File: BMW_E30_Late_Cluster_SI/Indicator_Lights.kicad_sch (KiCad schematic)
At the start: 20 parts, among them J1 SI LED Board, Q19 BC337-25, Q21 BC337-25, Q22 BC337-25, Q23 BC337-25, Y2 Crystal

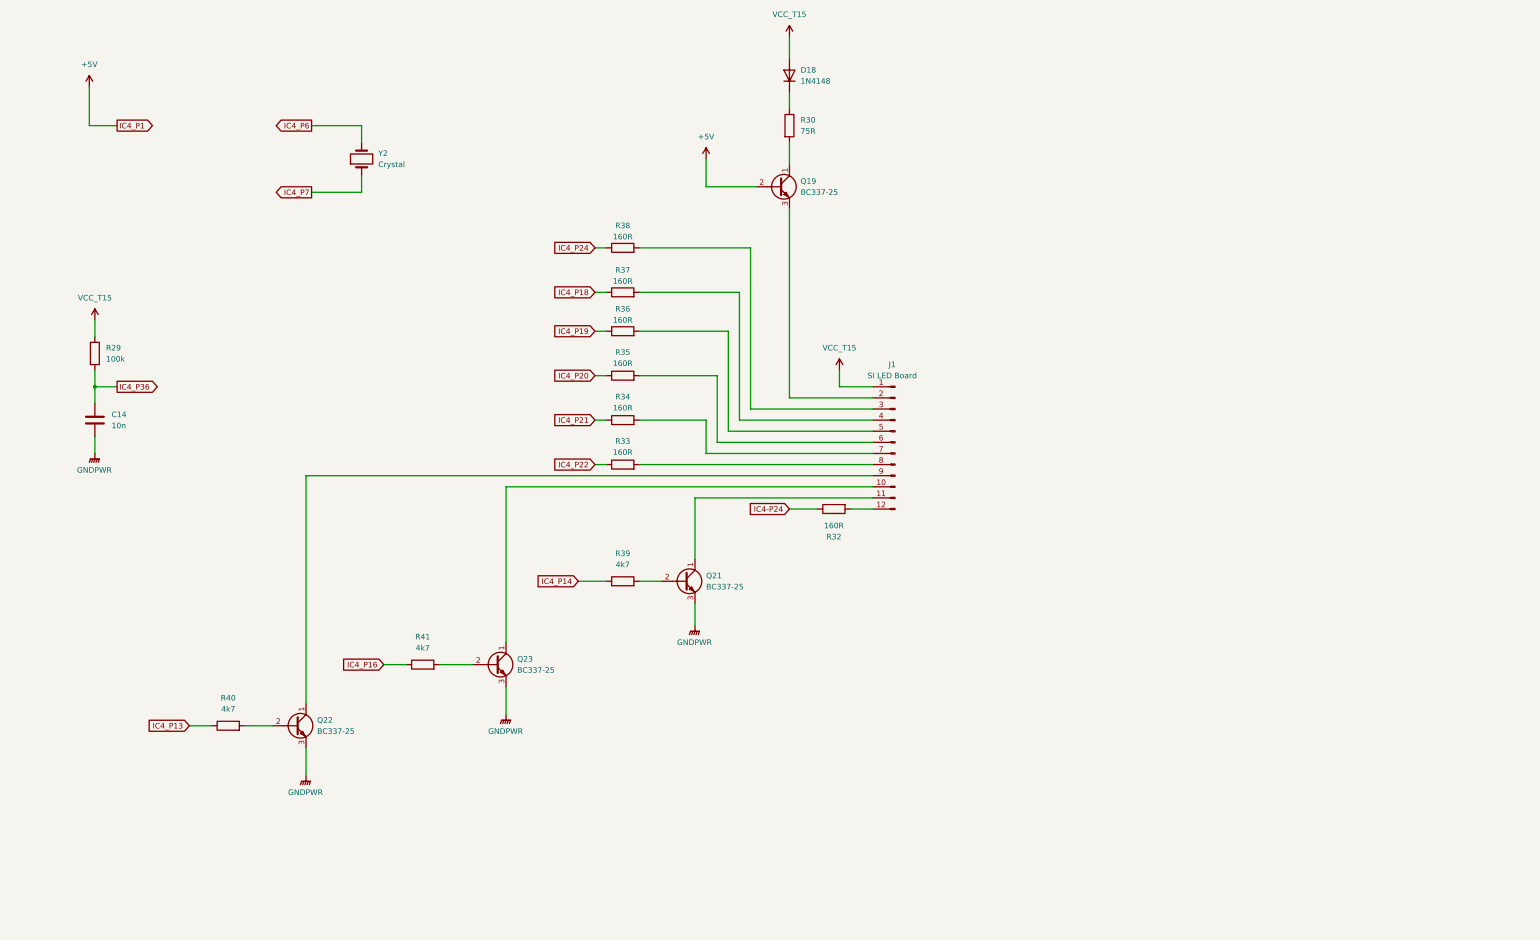
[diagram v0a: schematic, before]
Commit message: IC's Added to Schematic
IC's added, started going through IC2 (U2), pinouts not complete for these yet as many pins go between chips with no other components involved.
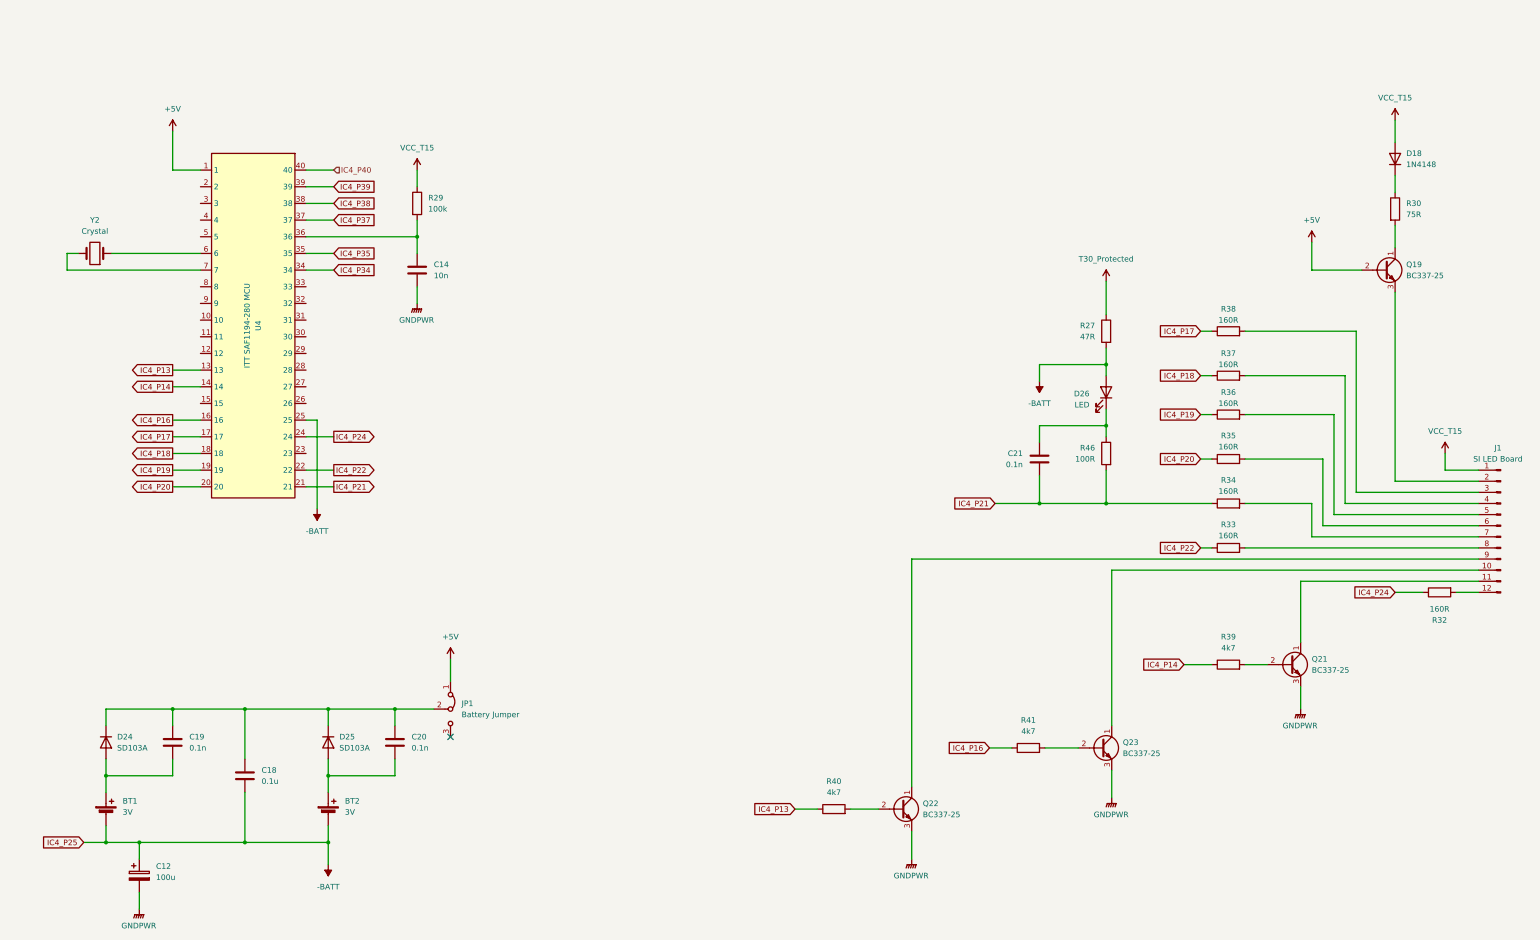
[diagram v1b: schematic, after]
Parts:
- added BT1, BT2: 3V, symbol Device:Battery_Cell
- added C12: 100u, Capacitor_THT:CP_Axial_L18.0mm_D6.5mm_P25.00mm_Horizontal, symbol Device:C_Polarized
- added C18: 0.1u, Capacitor_THT:C_Rect_L7.0mm_W2.0mm_P5.00mm, symbol Device:C
- added C19, C20, C21: 0.1n, Capacitor_THT:C_Disc_D6.0mm_W2.5mm_P5.00mm, symbol Device:C
- added D24, D25: SD103A, symbol Device:D
- added D26: LED, symbol Device:LED
- added JP1: Battery Jumper, symbol Jumper:Jumper_3_Bridged12
- added R27: 47R, Resistor_THT:R_Axial_DIN0516_L15.5mm_D5.0mm_P20.32mm_Horizontal, symbol Device:R
- added R46: 100R, SI_THT:R_Axial_Narrow_L6.8mm_D2.4mm_P9.7mm, symbol Device:R
- added U4: ITT SAF1194-280 MCU, Package_DIP:DIP-40_W15.24mm_LongPads, symbol BMW_ICs:ITT_SAF1194-280_MCU
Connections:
- net IC4-P24 is gone; now on net IC4_P24: R32.1
- net +5V: now also JP1.1 (A), U4.1
- net GNDPWR: now also C12.2
- net IC4_P13: now also U4.13
- net IC4_P14: now also U4.14
- net IC4_P16: now also U4.16
- net IC4_P18: now also U4.18
- net IC4_P19: now also U4.19
- net IC4_P20: now also U4.20
- net IC4_P21: now also C21.2, R46.2, U4.21
- net IC4_P22: now also U4.22
- net IC4_P24: now also U4.24; no longer R38.1
- net IC4_P36: no longer names the net of C14.1, R29.2
- net IC4_P36: now also U4.36
- net IC4_P6: no longer names the net of Y2.2
- net IC4_P6: now also U4.7
- net IC4_P7: no longer names the net of Y2.1
- net IC4_P7: now also U4.6
- new net: C21.1, D26.1 (K), R46.1
- new net: C18.1, C19.1, C20.1, D24.1 (K), D25.1 (K), JP1.2 (C)
- new net: BT2.1 (+), C20.2, D25.2 (A)
- new net: BT1.1 (+), C19.2, D24.2 (A)
- new net -BATT: BT1.2 (-), BT2.2 (-), C12.1, C18.2, D26.2 (A), R27.2, U4.25
- new net IC4_P17: R38.1, U4.17
- new net IC4_P34: U4.34
- new net IC4_P35: U4.35
- new net IC4_P37: U4.37
- new net IC4_P38: U4.38
- new net IC4_P39: U4.39
- new net IC4_P40: U4.40
- new net T30_Protected: R27.1
- no-connect marks 0 -> 1
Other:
- moved on the sheet: C14, D18, J1, Q19, Q21, Q22, Q23, R29, R30, R32, R33, R34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

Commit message: Schematic Functionally Complete
Only changes that should need to be made are formatting and style changes to improve readability.
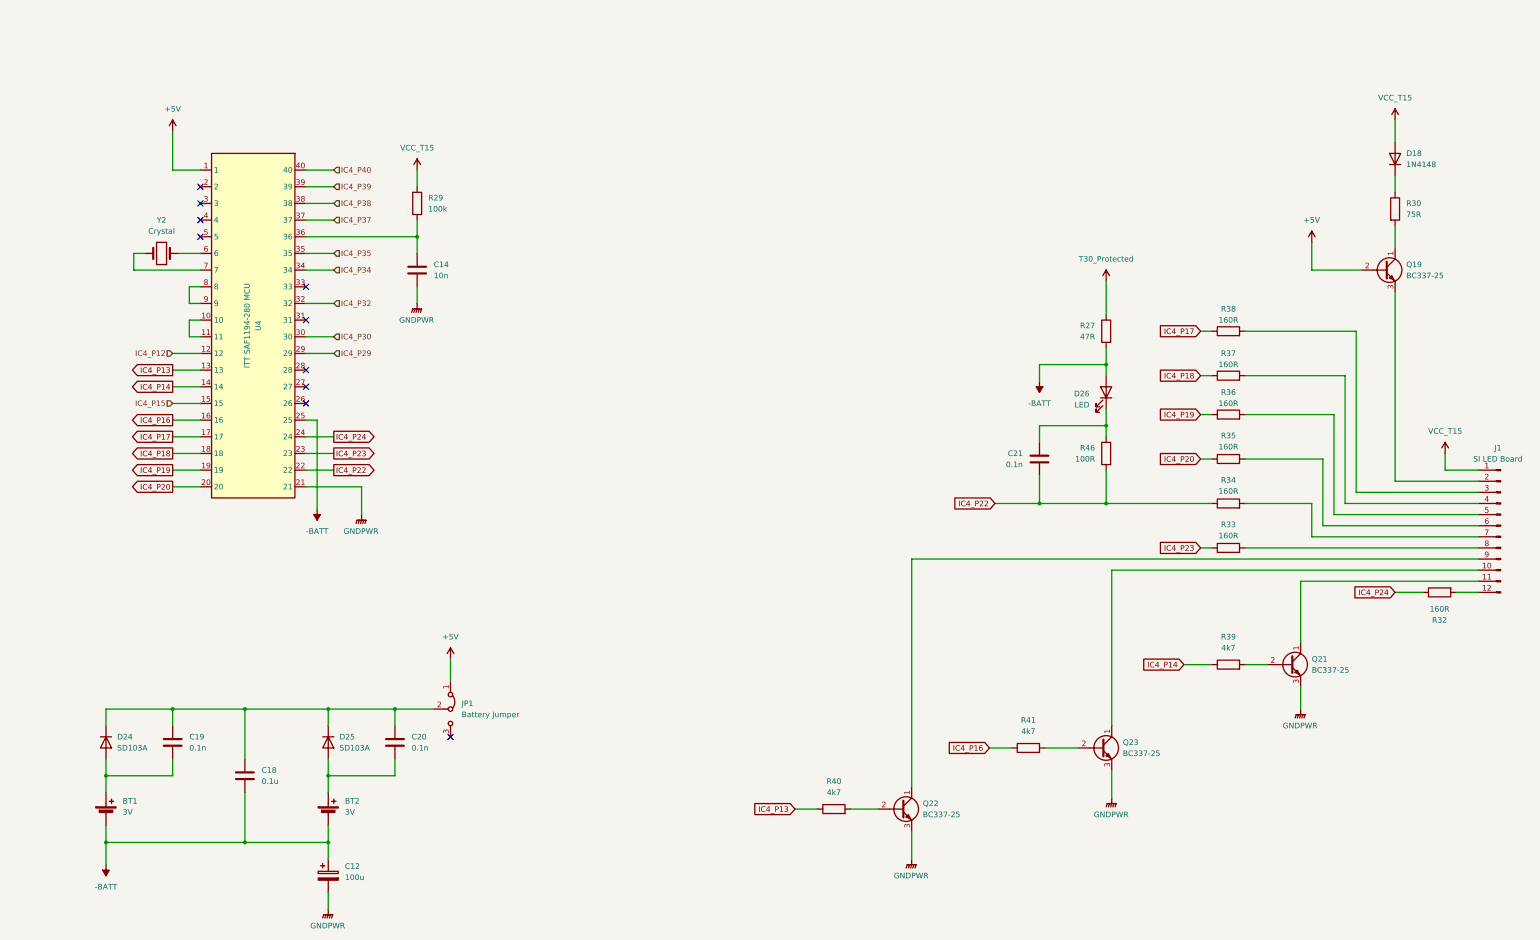
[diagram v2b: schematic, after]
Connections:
- net GNDPWR: now also U4.21
- net IC4_P22: now also C21.2, R34.1, R46.2; no longer R33.1
- net at U4.10: now also U4.11
- net IC4_P12: now reaches U4.12
- net IC4_P15: now reaches U4.15
- net IC4_P23: now reaches U4.23
- net IC4_P23: now also R33.1
- net IC4_P29: now reaches U4.29
- net IC4_P30: now reaches U4.30
- net IC4_P32: now reaches U4.32
- net at U4.8: now also U4.9
- removed net IC4_P21: C21.2, R34.1, R46.2, U4.21
- no-connect marks 1 -> 10
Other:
- moved on the sheet: C12, Y2

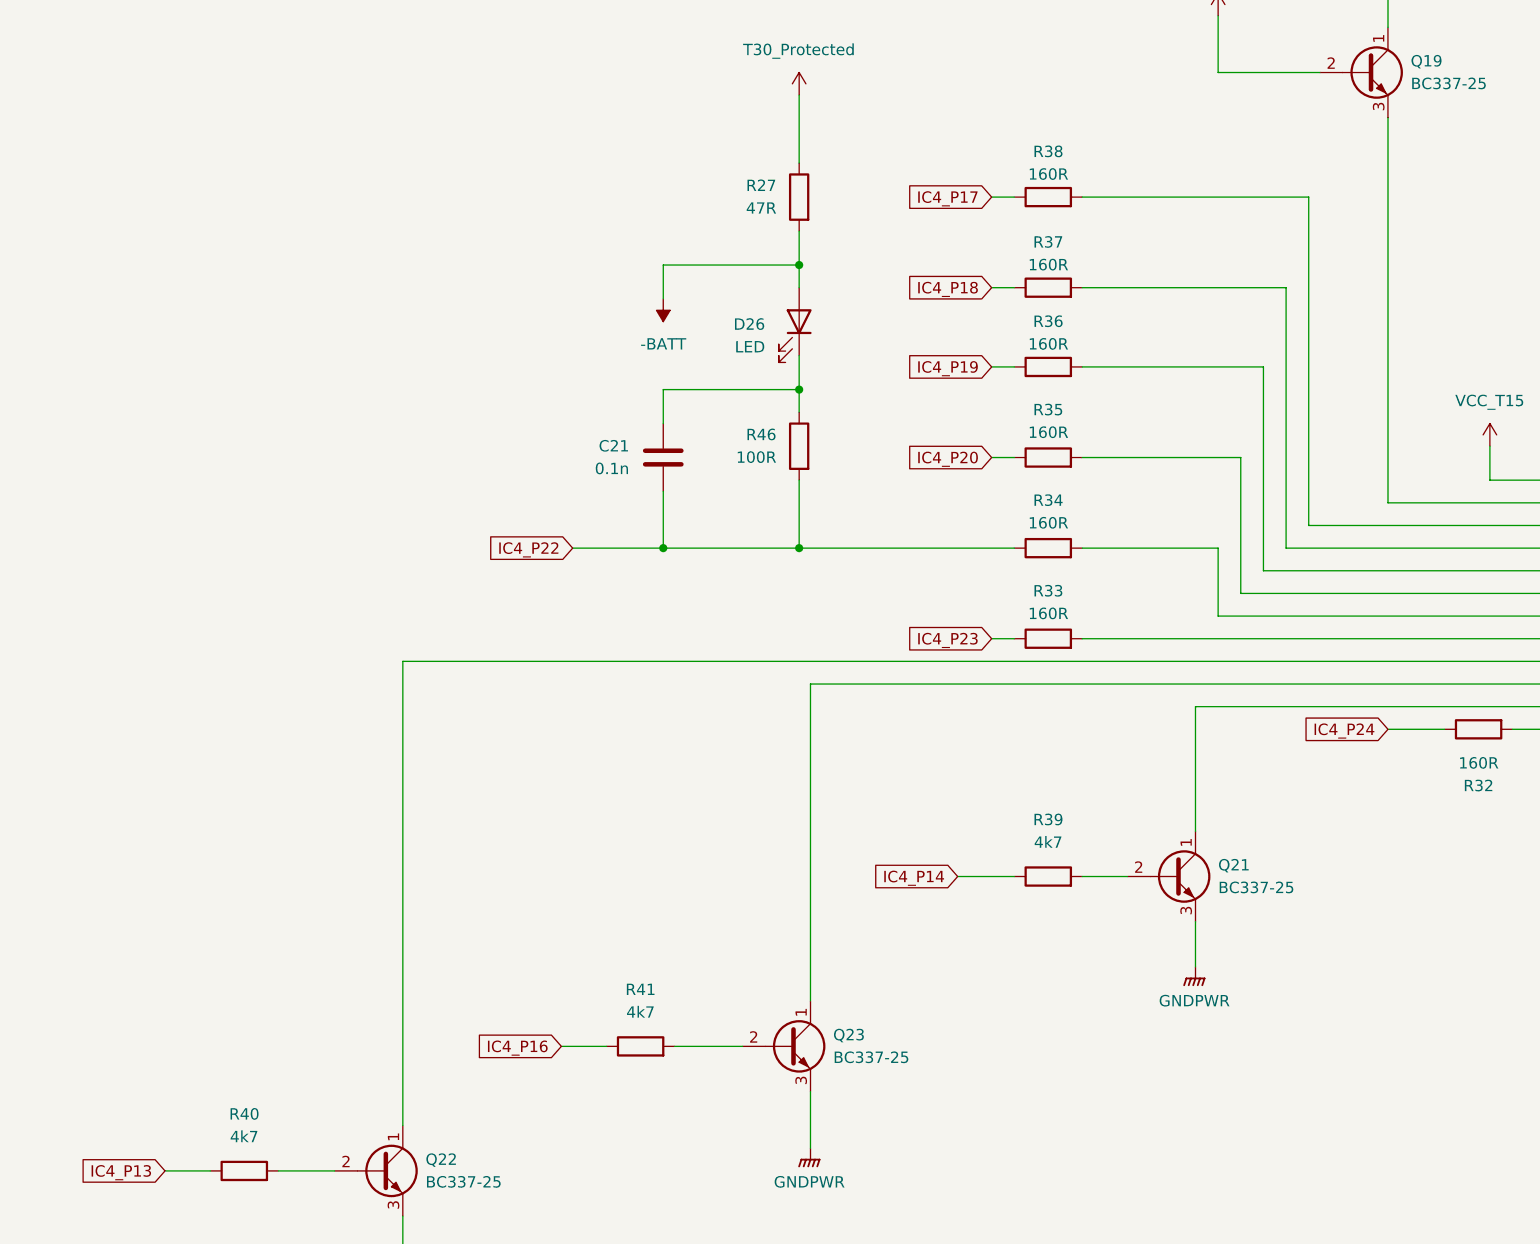
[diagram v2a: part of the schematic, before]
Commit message: Completed Schematic + Layout for SI LED
Additional labels were added to the SI board schematic to denote which pin controls which light on the LED board.
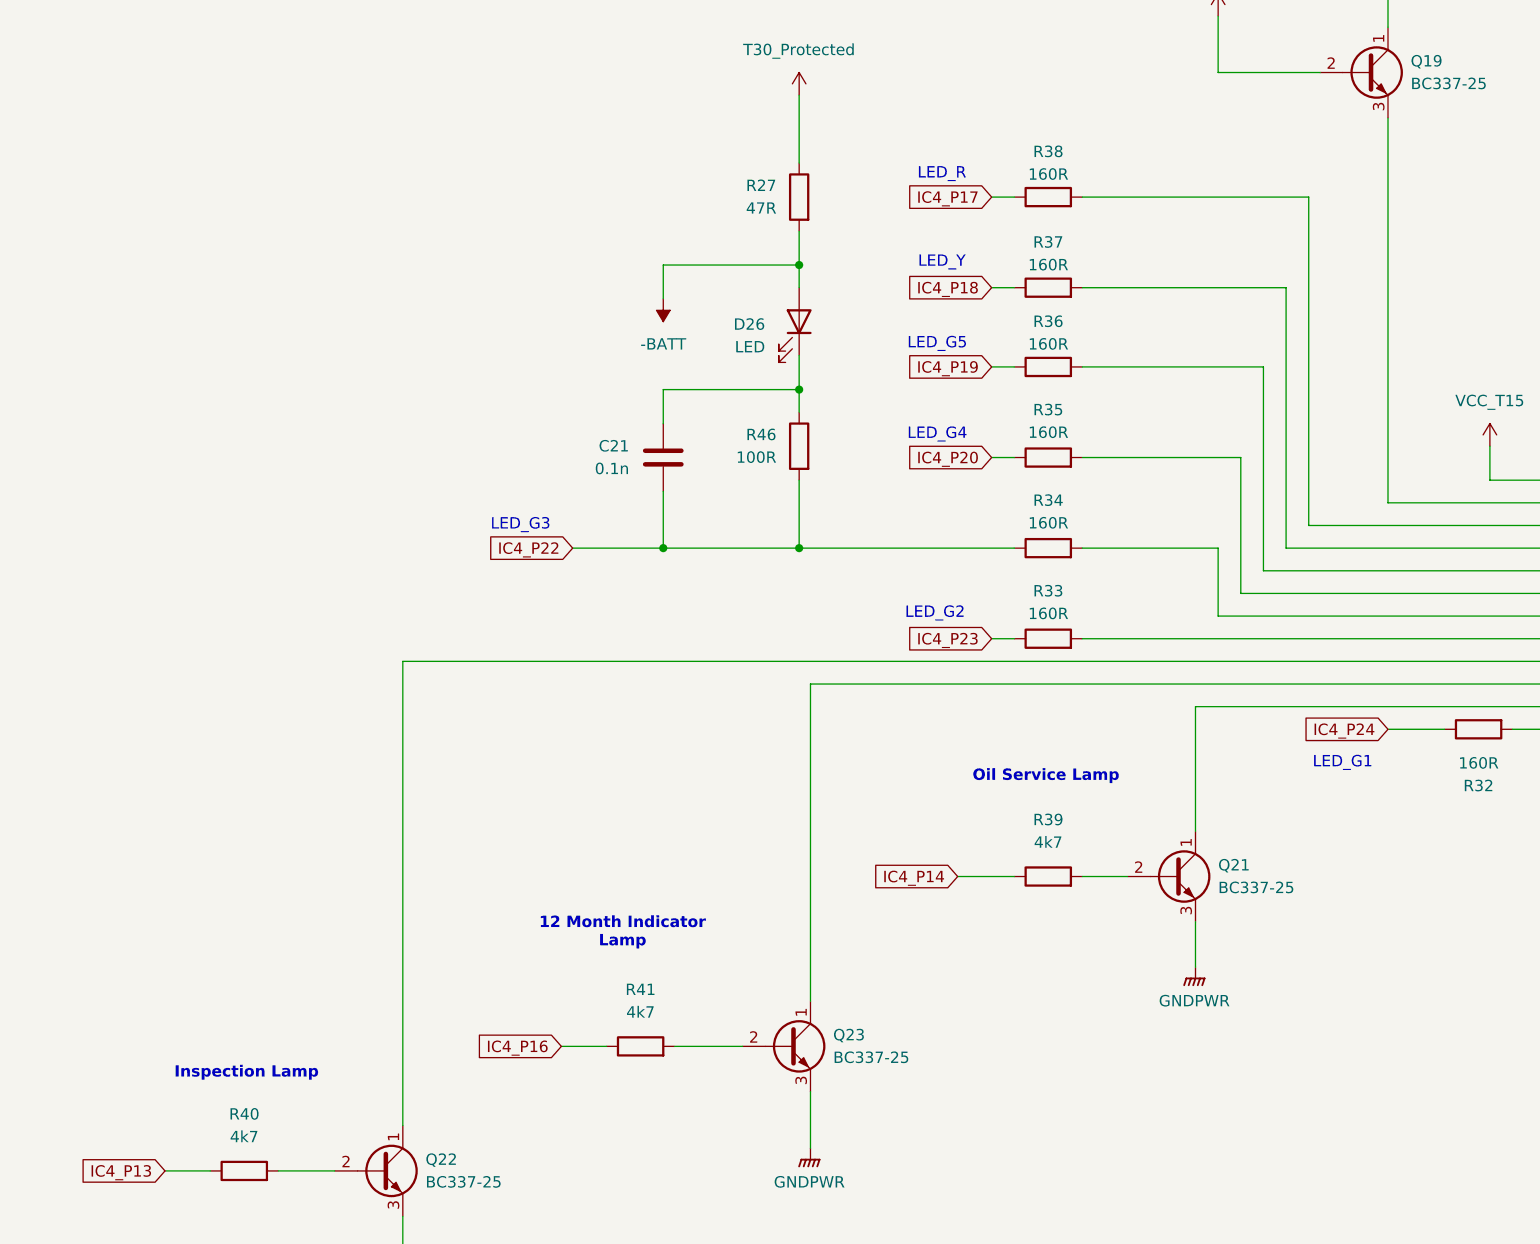
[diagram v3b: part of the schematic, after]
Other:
- note added: "12 Month Indicator Lamp"
- note added: "Inspection Lamp"
- note added: "LED_G1"
- note added: "LED_G2"
- note added: "LED_G3"
- note added: "LED_G4"
- note added: "LED_G5"
- note added: "LED_R"
- note added: "LED_Y"
- note added: "Oil Service Lamp"
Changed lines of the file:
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@@
 		(company "Reagan Ansel")
+	)
+	(text "Oil Service Lamp"
+		(exclude_from_sim no)
+		(at 300.736 152.654 0)
+		(effects
+			(font
+				(size 1.27 1.27)
+				(thickness 0.254)
+				(bold yes)
+			)
+		)
+	)
+	(text "LED_G1"
+		(exclude_from_sim no)
+		(at 334.01 151.13 0)
+		(effects
+			(font
+				(size 1.27 1.27)
+			)
+		)
+	)
+	(text "LED_G3"
+		(exclude_from_sim no)
+		(at 241.808 124.46 0)
+		(effects
+			(font
+				(size 1.27 1.27)
+			)
+		)
+	)
+	(text "LED_G5"
+		(exclude_from_sim no)
+		(at 288.544 104.14 0)
+		(effects
+			(font
+				(size 1.27 1.27)
+			)
+		)
+	)
+	(text "LED_R"
+		(exclude_from_sim no)
+		(at 289.052 85.09 0)
+		(effects
+			(font
+				(size 1.27 1.27)
+			)
+		)
+	)
+	(text "Inspection Lamp"
+		(exclude_from_sim no)
+		(at 211.074 185.928 0)
+		(effects
+			(font
+				(size 1.27 1.27)
+				(thickness 0.254)
+				(bold yes)
+			)
+		)
+	)
+	(text "LED_G2"
+		(exclude_from_sim no)
+		(at 288.29 134.366 0)
+		(effects
+			(font
+				(size 1.27 1.27)
+			)
+		)
+	)
+	(text "LED_Y"
+		(exclude_from_sim no)
+		(at 289.052 94.996 0)
+		(effects
+			(font
+				(size 1.27 1.27)
+			)
+		)
+	)
+	(text "12 Month Indicator\nLamp"
+		(exclude_from_sim no)
+		(at 253.238 170.18 0)
+		(effects
+			(font
+				(size 1.27 1.27)
+				(thickness 0.254)
+				(bold yes)
+			)
+		)
+	)
+	(text "LED_G4"
+		(exclude_from_sim no)
+		(at 288.544 114.3 0)
+		(effects
+			(font
+				(size 1.27 1.27)
+			)
+		)
 	)
 	(junction
@@
 	(wire
 		(pts
+			(xy 304.8 127) (xy 320.04 127)
+		)
+		(stroke
+			(width 0)
+			(type default)
+		)
+	)
+	(wire
+		(pts
 			(xy 358.14 129.54) (xy 325.12 129.54)
 		)
@@
 		)
 		(stroke
-			(width 0)
-			(type default)
-		)
-	)
-	(wire
-		(pts
-			(xy 304.8 127) (xy 320.04 127)
-		)
-		(stroke
